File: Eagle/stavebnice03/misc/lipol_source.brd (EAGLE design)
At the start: 25 parts

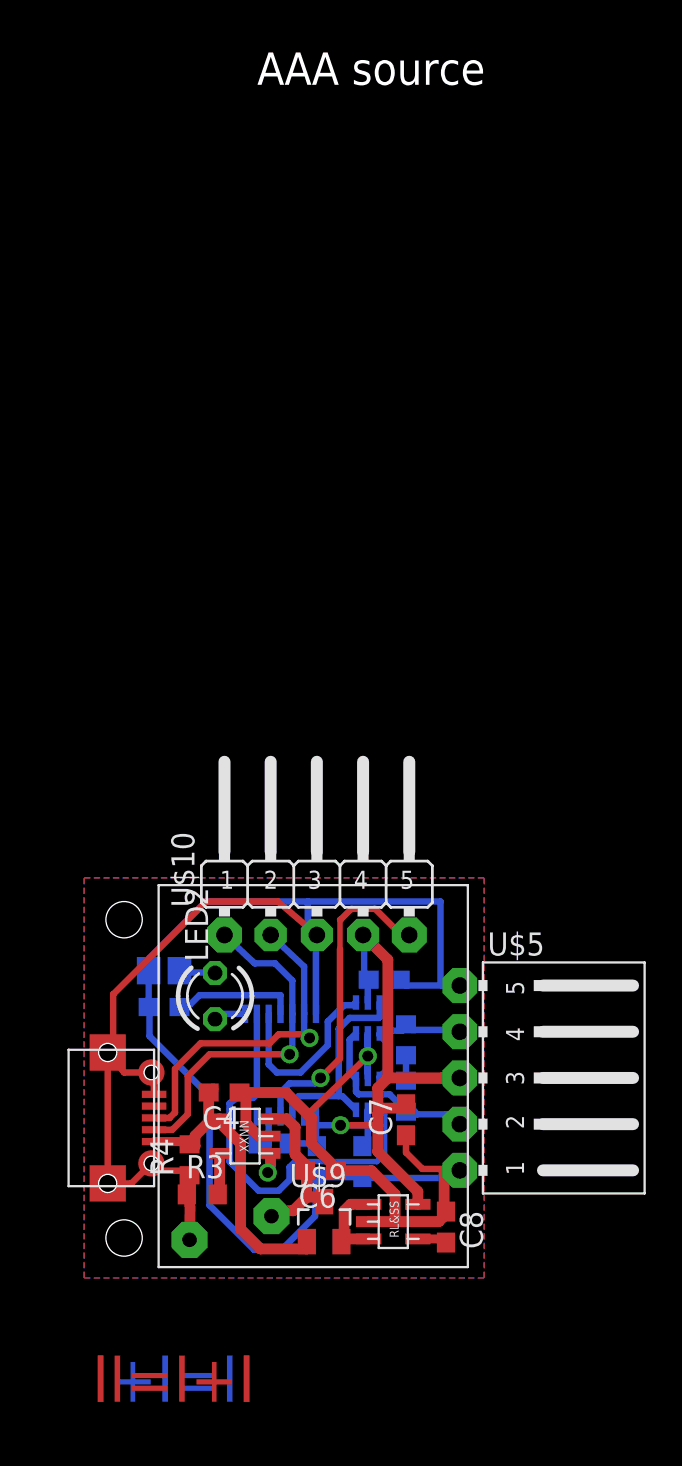
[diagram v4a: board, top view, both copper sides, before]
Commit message: added pin and resistor to stay in bootloader + changed size back to 21x21 mm
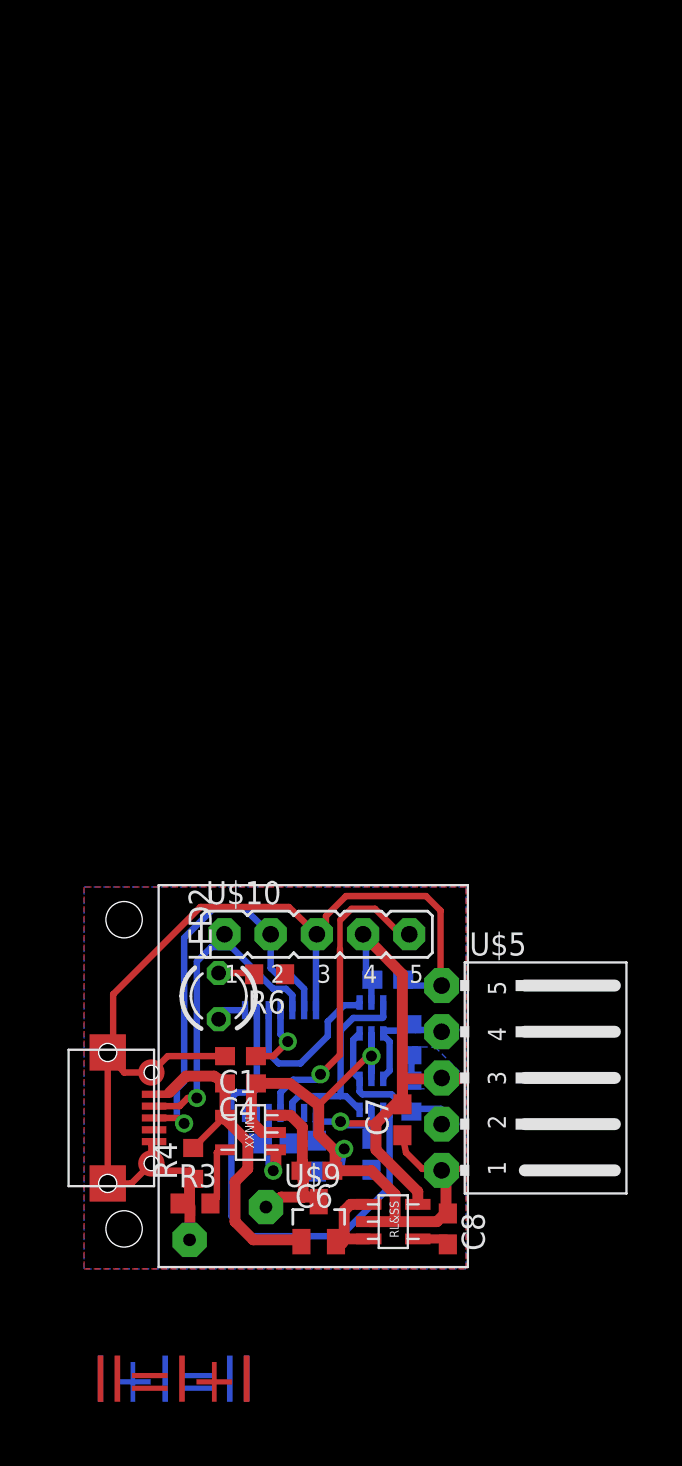
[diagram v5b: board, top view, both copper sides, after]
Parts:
- R6: device resistor:R0805 -> resistor:R0603
- U$10: value JUMPER5M-90 -> JUMPER5M; device !stavebnice03:JUMPER5M-90 -> !stavebnice03:JUMPER5M
- moved R6 5.80 mm to (10.2, 16.2), flipped to the top
- moved C1 4.99 mm to (8.60, 11.7), flipped to the top, turned to 180 degrees
- moved U$10 2.50 mm to (12.8, 18.4)
- moved C4 1.03 mm to (8.60, 10.2)
- moved U$5 1.00 mm to (22.2, 10.5)
- moved R3 0.64 mm to (6.10, 3.60)
- moved C5 0.64 mm to (15.8, 6.30)
- moved MCP73832 0.36 mm to (9.10, 7.50)
- moved R1 0.30 mm to (18.0, 9.50)
- moved R2 0.30 mm to (18.0, 12.6)
- moved C2 0.30 mm to (12.8, 6.20)
- moved U$9 0.30 mm to (12.9, 2.60)
- moved R4 0.28 mm to (6.00, 5.80)
- moved NC7SB3157P6X(1) 0.20 mm to (15.8, 9.60)
- moved NC7SB3157P6X(2) 0.20 mm to (15.8, 13.8)
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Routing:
- net GND: track 144.4 -> 108.8 mm, vias 1 -> 3
- net N$5: track 18.5 -> 23.6 mm
- net N$7: track 22.3 -> 27.1 mm
- net N$3: track 6.84 -> 3.97 mm, vias 0 -> 1
- net N$9: track 17.7 -> 20.5 mm
- net N$11: track 2.29 -> 3.50 mm
- net N$2: track 19.3 -> 18.3 mm
- net VCC: track 42.1 -> 42.8 mm
- net N$4: track 10.2 -> 9.53 mm
- added copper zone on layer 16, net VCC
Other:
- board text added: "Lipol source"
- board text removed: "AAA source"

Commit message: minor element position changes
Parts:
- moved R1 0.20 mm to (17.8, 9.50)
- moved R2 0.20 mm to (17.8, 12.6)
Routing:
- net VCC: track 42.8 -> 39.6 mm
- net N$6: track 10.5 -> 9.58 mm
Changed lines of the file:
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@@
 <layers>
 <layer number="1" name="Top" color="4" fill="1" visible="yes" active="yes"/>
-<layer number="16" name="Bottom" color="1" fill="1" visible="yes" active="yes"/>
+<layer number="16" name="Bottom" color="1" fill="1" visible="no" active="yes"/>
 <layer number="17" name="Pads" color="2" fill="1" visible="yes" active="yes"/>
 <layer number="18" name="Vias" color="2" fill="1" visible="yes" active="yes"/>
 <layer number="19" name="Unrouted" color="6" fill="1" visible="yes" active="yes"/>
 <layer number="20" name="Dimension" color="15" fill="1" visible="yes" active="yes"/>
-<layer number="21" name="tPlace" color="7" fill="1" visible="yes" active="yes"/>
-<layer number="22" name="bPlace" color="7" fill="1" visible="yes" active="yes"/>
+<layer number="21" name="tPlace" color="7" fill="1" visible="no" active="yes"/>
+<layer number="22" name="bPlace" color="7" fill="1" visible="no" active="yes"/>
 <layer number="23" name="tOrigins" color="15" fill="1" visible="yes" active="yes"/>
 <layer number="24" name="bOrigins" color="15" fill="1" visible="yes" active="yes"/>
@@
 <layer number="43" name="vRestrict" color="2" fill="10" visible="no" active="yes"/>
 <layer number="44" name="Drills" color="7" fill="1" visible="no" active="yes"/>
-<layer number="45" name="Holes" color="7" fill="1" visible="yes" active="yes"/>
+<layer number="45" name="Holes" color="7" fill="1" visible="no" active="yes"/>
 <layer number="46" name="Milling" color="3" fill="1" visible="no" active="yes"/>
 <layer number="47" name="Measures" color="7" fill="1" visible="no" active="yes"/>
@@
 <vertex x="13" y="2.8"/>
 </polygon>
-<wire x1="-2" y1="-2.5" x2="24" y2="-2.5" width="0.01" layer="49"/>
-<wire x1="24" y1="-2.5" x2="24" y2="23.5" width="0.01" layer="49"/>
-<wire x1="24" y1="23.5" x2="-2" y2="23.5" width="0.01" layer="49"/>
-<wire x1="-2" y1="23.5" x2="-2" y2="-2.5" width="0.01" layer="49"/>
-<text x="5.1" y="27.3" size="1.778" layer="49">Lipol source</text>
+<wire x1="-10" y1="-10" x2="31" y2="-10" width="0.01" layer="49"/>
+<wire x1="31" y1="-10" x2="31" y2="31" width="0.01" layer="49"/>
+<wire x1="31" y1="31" x2="-10" y2="31" width="0.01" layer="49"/>
+<wire x1="-10" y1="31" x2="-10" y2="-10" width="0.01" layer="49"/>
+<text x="10.5" y="27" size="1.778" layer="49" align="center">Lipol source</text>
 <circle x="2.2" y="19.2" radius="0.6" width="0.9" layer="116"/>
 <circle x="2.2" y="2.2" radius="0.6" width="0.9" layer="116"/>
@@
 <element name="U$1" library="!stavebnice03" package="TSSOP14" value="16F1454" x="10.8" y="11.4" rot="MR0"/>
 <element name="C2" library="resistor" package="C0603" value="100nF" x="12.8" y="6.2" rot="MR270"/>
-<element name="R1" library="resistor" package="R0603" value="2k2" x="18" y="9.5" rot="MR90"/>
-<element name="R2" library="resistor" package="R0603" value="2k2" x="18" y="12.6" rot="MR270"/>
+<element name="R1" library="resistor" package="R0603" value="2k2" x="17.8" y="9.5" rot="MR90"/>
+<element name="R2" library="resistor" package="R0603" value="2k2" x="17.8" y="12.6" rot="MR270"/>
 <element name="C3" library="resistor" package="C0603" value="100nF" x="16.7" y="15.9" rot="MR0"/>
 <element name="U$5" library="!stavebnice03" package="JUMPER5F-90" value="JUMPER5F-90" x="22.2" y="10.5" rot="R270"/>
@@
 <wire x1="7.75" y1="11.7" x2="4.6" y2="11.7" width="0.357" layer="1"/>
 <wire x1="4.6" y1="11.7" x2="3.7" y2="10.8" width="0.357" layer="1"/>
-<wire x1="12.8" y1="5.35" x2="14.1" y2="5.35" width="0.357" layer="16"/>
-<wire x1="14.1" y1="5.35" x2="15.8" y2="5.45" width="0.357" layer="16"/>
-<wire x1="15.8" y1="5.45" x2="15.3" y2="5.4" width="0.357" layer="16"/>
+<wire x1="12.8" y1="5.35" x2="14.3" y2="5.35" width="0.357" layer="16"/>
+<wire x1="14.3" y1="5.35" x2="15.8" y2="5.45" width="0.357" layer="16"/>
+<wire x1="15.8" y1="5.45" x2="15.8" y2="5.5" width="0.357" layer="16"/>
 <via x="14.3" y="6.6" extent="1-16" drill="0.6"/>
-<wire x1="14.1" y1="5.35" x2="14.3" y2="6.6" width="0.357" layer="16"/>
+<wire x1="14.3" y1="5.35" x2="14.3" y2="6.6" width="0.357" layer="16"/>
 <wire x1="13.8" y1="6.5" x2="13.8" y2="6.1" width="0.357" layer="1"/>
 <wire x1="13.8" y1="6.1" x2="13.9" y2="6" width="0.357" layer="1"/>
@@
 <wire x1="12.75" y1="7.2" x2="12.8" y2="7.05" width="0.3556" layer="16"/>
 <wire x1="14.1" y1="8.1" x2="12.75" y2="8.1" width="0.3556" layer="16"/>
-<wire x1="18" y1="10.35" x2="18" y2="11.75" width="0.3556" layer="16"/>
+<wire x1="17.8" y1="10.35" x2="17.8" y2="11.75" width="0.3556" layer="16"/>
 <contactref element="TC1185" pad="VOUT"/>
 <contactref element="C7" pad="2"/>
@@
 <wire x1="16.05" y1="8" x2="16.05" y2="6.55" width="0.6" layer="1"/>
 <wire x1="18.35" y1="4.25" x2="16.05" y2="6.55" width="0.6" layer="1"/>
-<wire x1="20.51" y1="10.35" x2="18" y2="10.35" width="0.3556" layer="16"/>
+<wire x1="19.51" y1="10.35" x2="17.8" y2="10.35" width="0.3556" layer="16"/>
 <wire x1="15.8" y1="14.65" x2="15.8" y2="15.85" width="0.3556" layer="16"/>
 <wire x1="15.8" y1="15.85" x2="15.85" y2="15.9" width="0.3556" layer="16"/>
@@
 <wire x1="12.55" y1="6.9" x2="12.8" y2="7.05" width="0.3556" layer="16"/>
 <wire x1="15.85" y1="15.9" x2="15.7" y2="15.9" width="0.3556" layer="16"/>
-<wire x1="20.51" y1="10.35" x2="19.66" y2="10.5" width="0.3556" layer="16"/>
+<wire x1="19.51" y1="10.35" x2="19.66" y2="10.5" width="0.3556" layer="16"/>
 <wire x1="17.19" y1="9.14" x2="16.05" y2="8" width="0.6" layer="1"/>
 <wire x1="17.5" y1="16.2" x2="17.5" y2="9.05" width="0.6" layer="1"/>
 <wire x1="17.5" y1="9.05" x2="17.51" y2="10.45" width="0.6" layer="1"/>
-<wire x1="17.51" y1="10.45" x2="20.61" y2="10.45" width="0.6" layer="1"/>
-<wire x1="20.61" y1="10.45" x2="19.66" y2="10.5" width="0.6" layer="1"/>
+<wire x1="17.51" y1="10.45" x2="19.71" y2="10.45" width="0.6" layer="1"/>
+<wire x1="19.71" y1="10.45" x2="19.66" y2="10.5" width="0.6" layer="1"/>
 <wire x1="17.19" y1="9.14" x2="17.69" y2="9.04" width="0.357" layer="1"/>
 <wire x1="17.69" y1="9.04" x2="17.5" y2="9.05" width="0.357" layer="1"/>
@@
 <wire x1="16.45" y1="12.95" x2="16.45" y2="12.85" width="0.3556" layer="16"/>
 <wire x1="16.45" y1="12.85" x2="16.8" y2="12.5" width="0.3556" layer="16"/>
-<wire x1="18.21" y1="13.14" x2="18" y2="13.45" width="0.3556" layer="16"/>
-<wire x1="18" y1="13.45" x2="17.9" y2="13.3" width="0.3556" layer="16"/>
+<wire x1="18.21" y1="13.14" x2="17.8" y2="13.45" width="0.3556" layer="16"/>
+<wire x1="17.8" y1="13.45" x2="17.9" y2="13.3" width="0.3556" layer="16"/>
 <wire x1="17.9" y1="13.3" x2="17.7" y2="13.1" width="0.3556" layer="16"/>
 <wire x1="18.21" y1="13.14" x2="20.46" y2="13.14" width="0.3556" layer="16"/>
@@
 <wire x1="14.8" y1="12.6" x2="14.8" y2="10.795" width="0.357" layer="16"/>
 <wire x1="14.8" y1="10.795" x2="15.15" y2="10.45" width="0.357" layer="16"/>
-<wire x1="18" y1="8.65" x2="18.1" y2="8.8" width="0.3556" layer="16"/>
+<wire x1="17.8" y1="8.65" x2="18.1" y2="8.8" width="0.3556" layer="16"/>
 <wire x1="18.1" y1="8.8" x2="19.62" y2="8.8" width="0.3556" layer="16"/>
-<wire x1="18" y1="8.65" x2="17.95" y2="8.75" width="0.3556" layer="16"/>
+<wire x1="17.8" y1="8.65" x2="17.95" y2="8.75" width="0.3556" layer="16"/>
 <wire x1="17.95" y1="8.75" x2="17.9" y2="8.8" width="0.3556" layer="16"/>
 <wire x1="17.9" y1="8.8" x2="17.7" y2="8.8" width="0.3556" layer="16"/>
@@
 <wire x1="15.15" y1="9.75" x2="15.3" y2="9.6" width="0.3556" layer="16"/>
 <wire x1="15.3" y1="9.6" x2="16.9" y2="9.6" width="0.3556" layer="16"/>
-<wire x1="20.46" y1="7.96" x2="19.66" y2="7.96" width="0.3556" layer="16"/>
-<wire x1="19.62" y1="8.8" x2="20.46" y2="7.96" width="0.3556" layer="16"/>
+<wire x1="19.66" y1="8.06" x2="19.66" y2="7.96" width="0.3556" layer="16"/>
+<wire x1="19.62" y1="8.8" x2="19.66" y2="8.06" width="0.3556" layer="16"/>
 </signal>
 <signal name="N$7">
@@
 <wire x1="10.7" y1="16.1" x2="10.26" y2="16.54" width="0.357" layer="16"/>
 <wire x1="10.26" y1="16.54" x2="10.26" y2="18.4" width="0.357" layer="16"/>
-<wire x1="8.82" y1="19.8" x2="10.26" y2="18.4" width="0.357" layer="16"/>
 <wire x1="5.5" y1="10.3" x2="5.5" y2="18.2" width="0.3556" layer="16"/>
 <wire x1="5.5" y1="18.2" x2="7.1" y2="19.8" width="0.3556" layer="16"/>
-<wire x1="7.1" y1="19.8" x2="8.82" y2="19.8" width="0.3556" layer="16"/>
+<wire x1="7.1" y1="19.8" x2="8.4" y2="19.8" width="0.3556" layer="16"/>
+<wire x1="8.4" y1="19.8" x2="9.7" y2="18.5" width="0.3556" layer="16"/>
+<wire x1="9.7" y1="18.5" x2="10.16" y2="18.5" width="0.3556" layer="16"/>
+<wire x1="10.16" y1="18.5" x2="10.26" y2="18.4" width="0.3556" layer="16"/>
 </signal>
 <signal name="N$3">

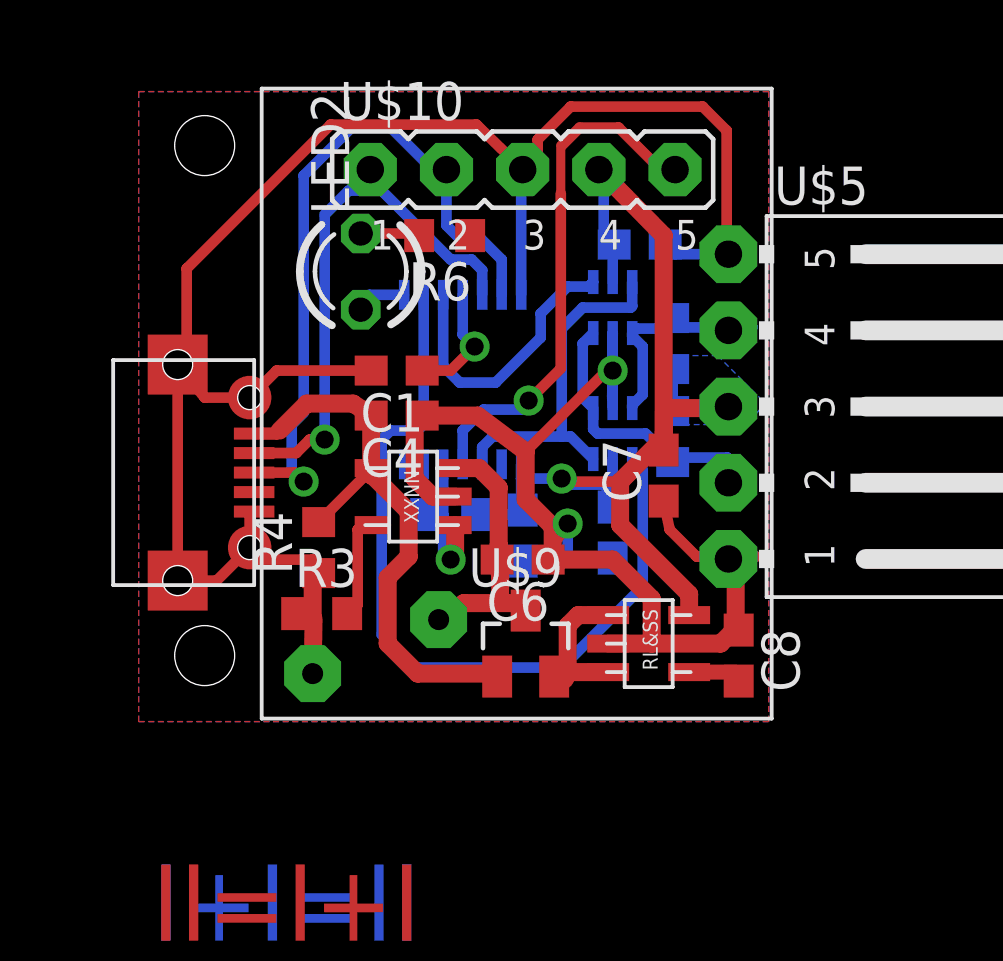
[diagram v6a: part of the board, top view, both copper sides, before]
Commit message: fix of bugs on rgb and lipol board + a few minor changes
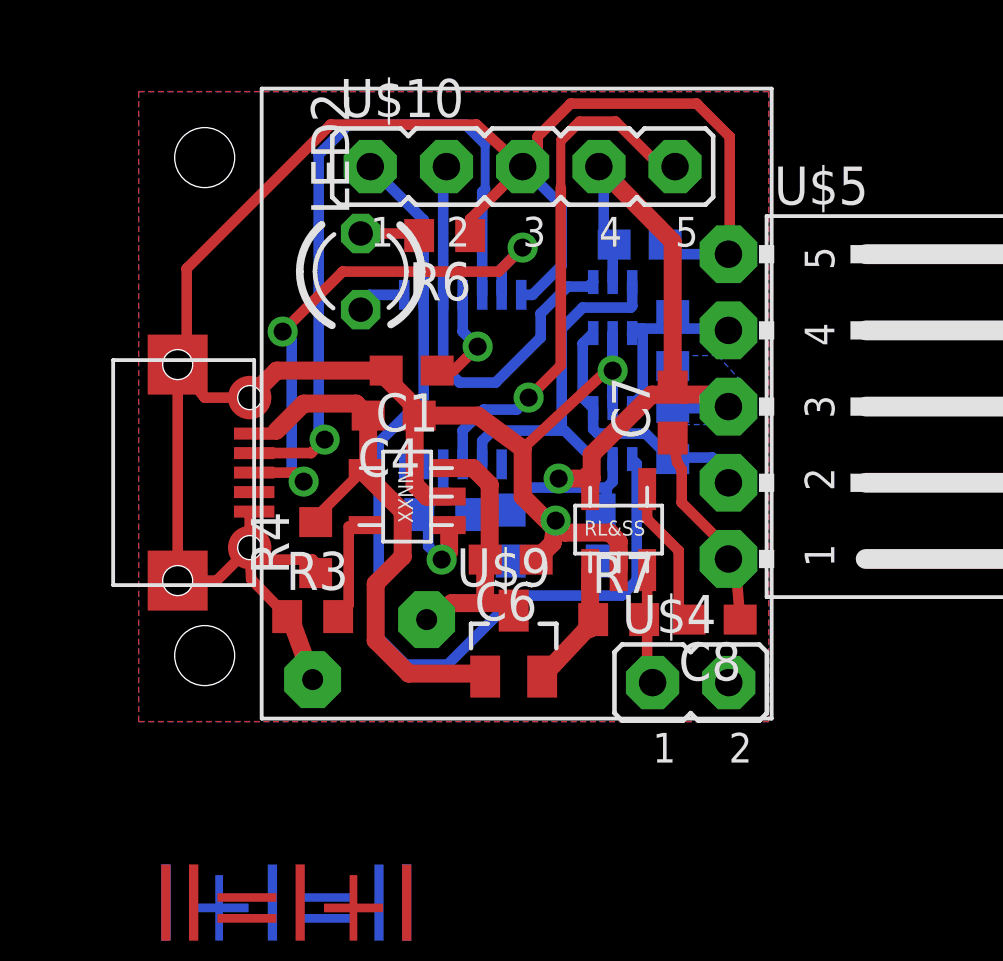
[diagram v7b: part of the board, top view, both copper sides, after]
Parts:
- added R7: 100k, resistor:R0603
- added U$4: JUMPER2M, !stavebnice03:JUMPER2M
- moved TC1185 3.93 mm to (16.0, 6.40), turned to 0 degrees
- moved C7 2.12 mm to (17.8, 10.3)
- moved C8 1.44 mm to (19.2, 3.40), turned to 180 degrees
- moved C1 0.50 mm to (9.10, 11.7)
- moved C5 0.41 mm to (15.4, 6.20)
- moved C2 0.40 mm to (12.4, 6.20)
- moved C6 0.40 mm to (12.4, 5.40)
- moved U$9 0.40 mm to (12.5, 2.60)
- moved R3 0.32 mm to (5.80, 3.50)
- moved R5 0.20 mm to (10.2, 6.90)
- moved MCP73832 0.20 mm to (8.90, 7.50)
- moved U$10 0.10 mm to (12.8, 18.5)
- moved C4 0.10 mm to (8.50, 10.2)
- moved R1 0.10 mm to (17.8, 9.60)
- moved R2 0.10 mm to (17.8, 12.7)
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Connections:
- new net N$20: R7.2, TC1185.SHDN, U$4.1
- net GND: now also U$4.2
- net N$12: now also R7.1; no longer TC1185.SHDN
- net N$2: no longer U$10.1
- net N$4: now also U$10.2
- net N$5: no longer U$10.2
- net N$7: now also U$10.1
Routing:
- net VCC: track 39.6 -> 33.0 mm
- net N$5: track 23.7 -> 18.1 mm, vias 1 -> 3
- net GND: track 108.3 -> 102.9 mm, vias 3 -> 2
- net N$2: track 18.3 -> 23.4 mm
- net N$4: track 9.53 -> 13.9 mm
- net N$7: track 27.1 -> 31.3 mm
- net N$20: track 0.00 -> 4.05 mm
- net N$17: track 1.87 -> 4.91 mm
- net N$10: track 8.14 -> 6.64 mm
- net N$12: track 5.52 -> 4.58 mm
- net N$11: track 3.50 -> 4.01 mm

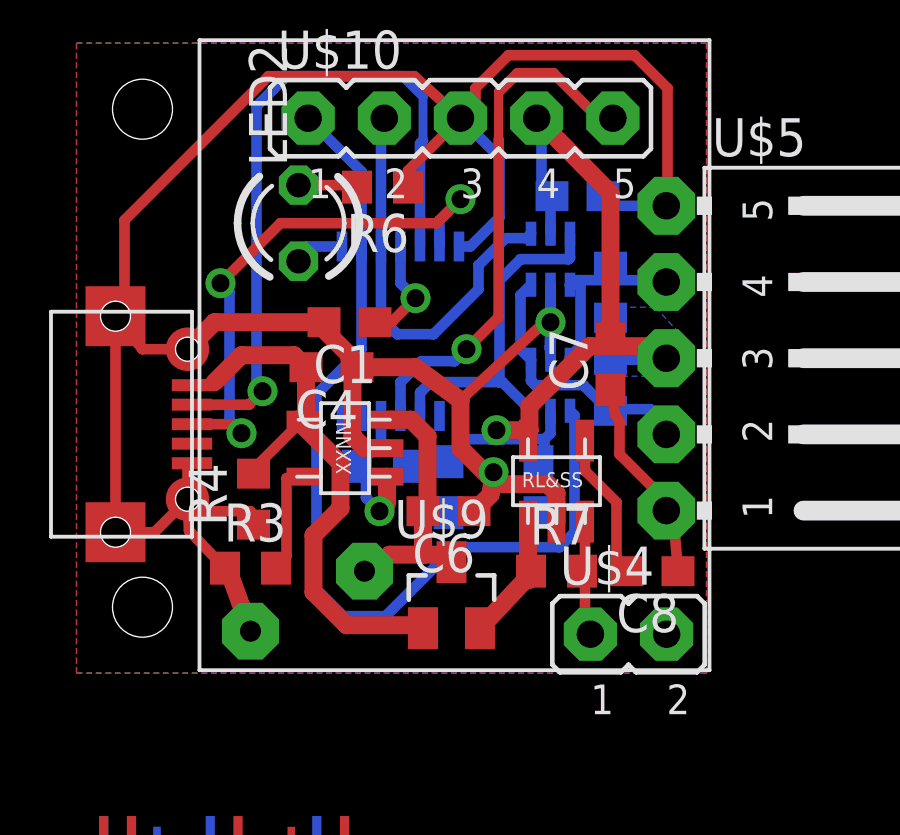
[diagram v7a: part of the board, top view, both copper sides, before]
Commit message: C0603 changed to C0603K with wider space between soldering areas
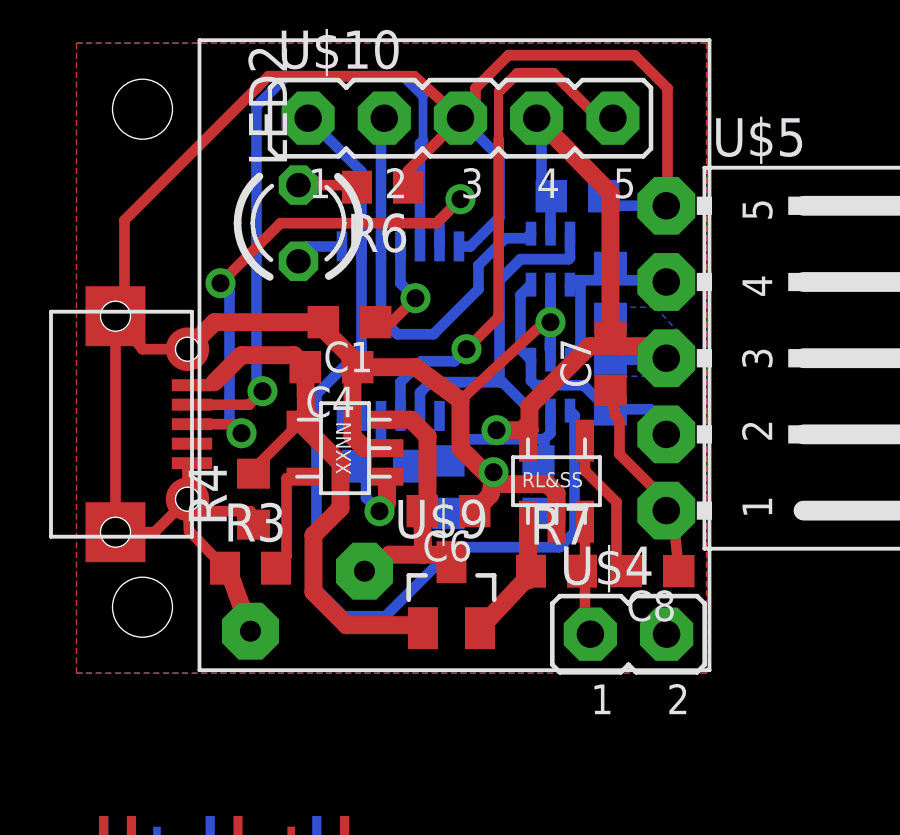
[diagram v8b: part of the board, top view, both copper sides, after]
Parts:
- C1, C2, C3, C4, C5, C6, C7, C8: device resistor:C0603 -> resistor:C0603K
